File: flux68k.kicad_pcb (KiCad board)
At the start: 2 copper layers, 100 x 50 mm, 27 parts, among them J1 Conn_02x17_Odd_Even, J2 Conn_02x17_Odd_Even, J3 Conn_01x04, J4 Conn_01x04, J5 DB37_Female_MountingHoles, J6 Barrel_Jack, J7 Conn_01x01, J8 Conn_01x01, SW1 SW_SPDT, U1 74LS06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

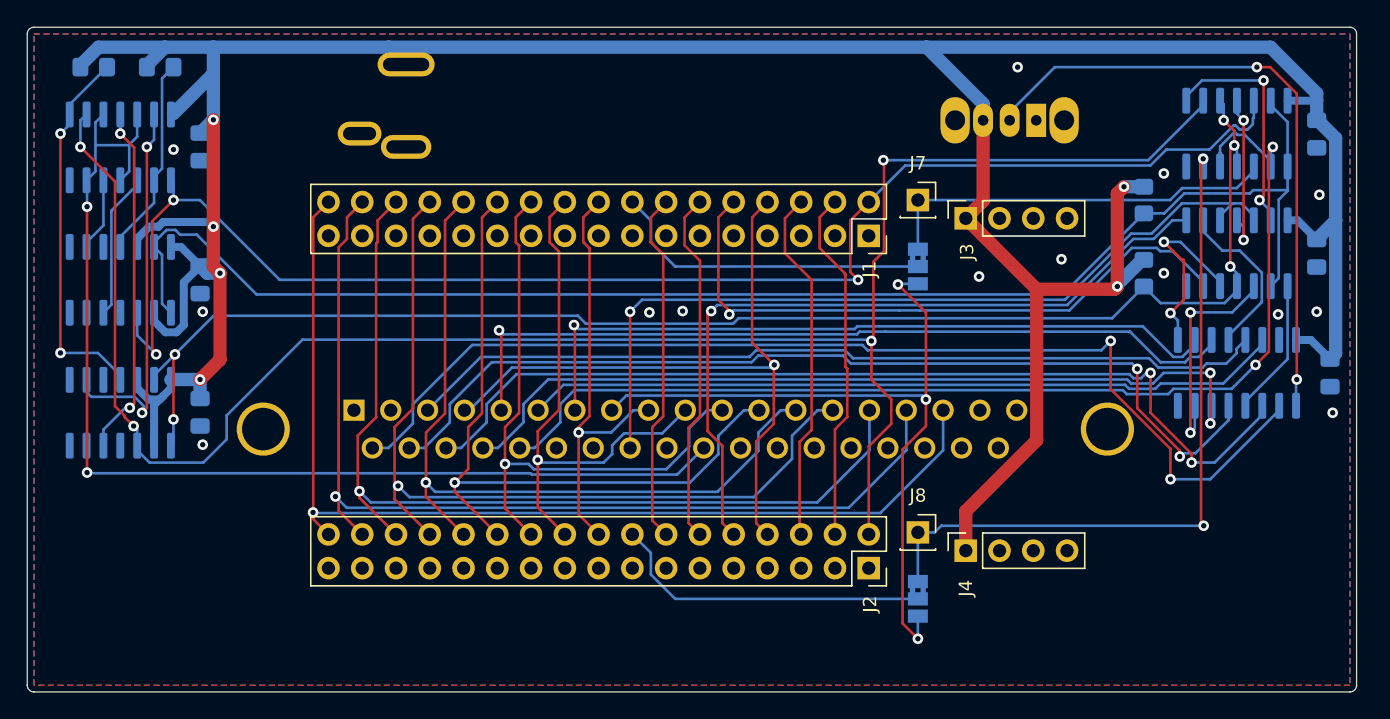
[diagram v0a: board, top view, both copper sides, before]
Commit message: add pullups and ideal diodes to flux68k
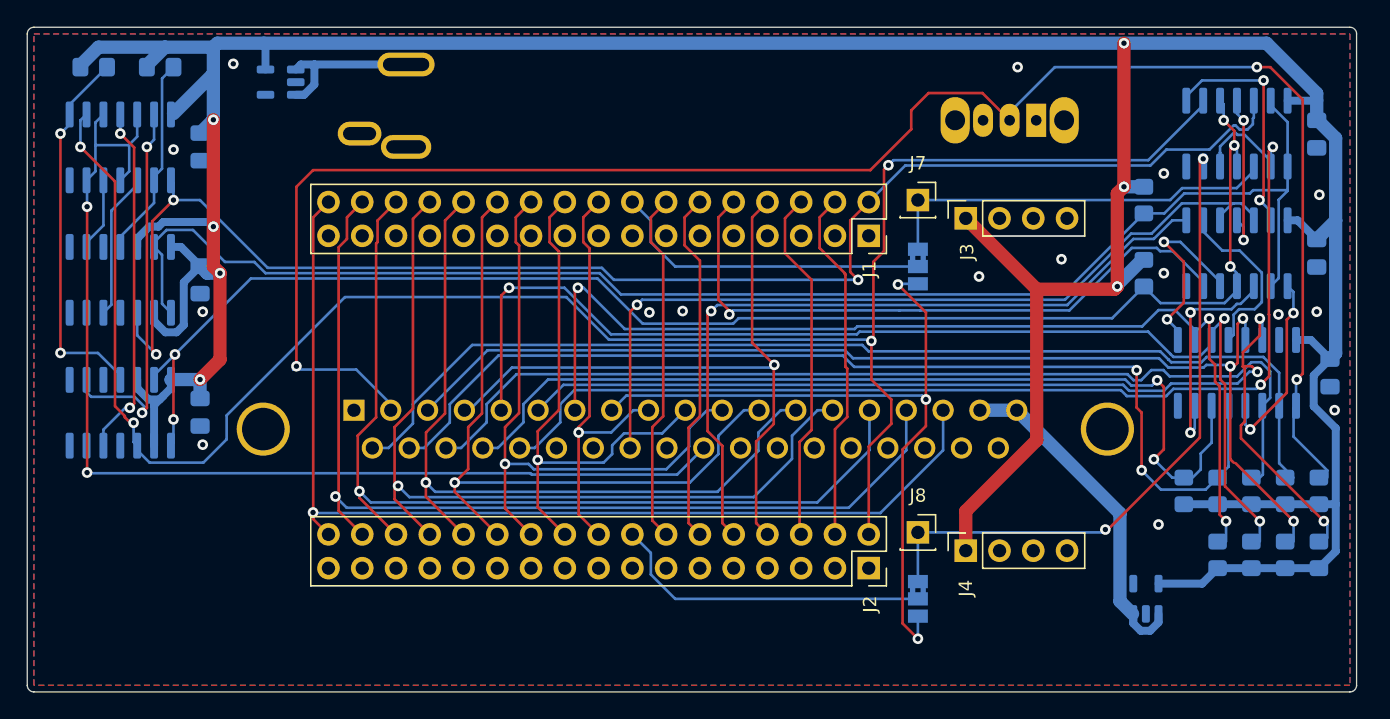
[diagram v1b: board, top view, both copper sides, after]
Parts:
- added R10: 10k, Resistor_SMD:R_0805_2012Metric_Pad1.20x1.40mm_HandSolder, B.Cu at (177.2, 59.7)
- added R11: 10k, Resistor_SMD:R_0805_2012Metric_Pad1.20x1.40mm_HandSolder, B.Cu at (169.5, 59.7)
- added R12: 10k, Resistor_SMD:R_0805_2012Metric_Pad1.20x1.40mm_HandSolder, B.Cu at (172.1, 59.7)
- added R13: 10k, Resistor_SMD:R_0805_2012Metric_Pad1.20x1.40mm_HandSolder, B.Cu at (177.2, 54.9)
- added R5: 10k, Resistor_SMD:R_0805_2012Metric_Pad1.20x1.40mm_HandSolder, B.Cu at (174.6, 54.9)
- added R6: 10k, Resistor_SMD:R_0805_2012Metric_Pad1.20x1.40mm_HandSolder, B.Cu at (172.1, 54.9)
- added R7: 10k, Resistor_SMD:R_0805_2012Metric_Pad1.20x1.40mm_HandSolder, B.Cu at (169.5, 54.9)
- added R8: 10k, Resistor_SMD:R_0805_2012Metric_Pad1.20x1.40mm_HandSolder, B.Cu at (167.0, 54.9)
- added R9: 10k, Resistor_SMD:R_0805_2012Metric_Pad1.20x1.40mm_HandSolder, B.Cu at (174.6, 59.7)
- added U7: MAX40200AUK, Package_TO_SOT_SMD:SOT-23-5, B.Cu at (99.1, 24.1)
- added U8: MAX40200AUK, Package_TO_SOT_SMD:SOT-23-5, B.Cu at (164.2, 63.0)
- U2: value 74LS32 -> 74HCT32
- U3, U4: value 74LS74 -> 74HCT74
- U6: value 74LS157 -> 74HCT157
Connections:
- J5 pad 18: unconnected-(J5-Pad18) -> /VIN_DB37
- J5 pad 19: unconnected-(J5-Pad19) -> /VIN_DB37
- J5 pad 2: unconnected-(J5-Pad2) -> /~{SWAP}
- J6 pad 1: +5V -> /VIN_BARREL
- SW1 pad 2: Net-(SW1-Pad2) -> /~{SWAP}
- SW1 pad 3: +5V -> unconnected-(SW1-C-Pad3)
- U6 pad 1: Net-(SW1-Pad2) -> /~{SWAP}
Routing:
- net /~{SWAP}: track 0.00 -> 136.0 mm, vias 0 -> 3
- net Net-(SW1-Pad2): track 47.9 -> 0.00 mm, vias 2 -> 0
- net +5V: track 256.4 -> 293.9 mm, vias 6 -> 7
- net /VIN_DB37: track 0.00 -> 25.4 mm
- net /~{X68K_DS0}: track 61.7 -> 85.5 mm, vias 1 -> 3
- net /~{X68K_DS2}: track 55.0 -> 78.3 mm, vias 1 -> 3
- net /~{X68K_DS1}: track 57.1 -> 78.5 mm, vias 0 -> 3
- net /~{X68K_DS3}: track 65.0 -> 83.8 mm, vias 0 -> 3
- net /VIN_BARREL: track 0.00 -> 11.7 mm
- net /~{OPTION1}: track 72.7 -> 79.0 mm
- net /~{OPTION3}: track 63.3 -> 69.3 mm
- net /~{BOTTOM_EJECT}: track 53.7 -> 49.5 mm
- net Net-(U6-Za): track 10.3 -> 14.2 mm, vias 0 -> 2
- net /~{OPTION2}: track 71.9 -> 74.9 mm, vias 2 -> 0
- net /~{BOTTOM_DCD}: track 143.8 -> 146.2 mm
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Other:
- board text added: "TD-FluX68K v1.1"
- board text removed: "TD-FluX68K v1.0"

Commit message: shrink board by 1mm
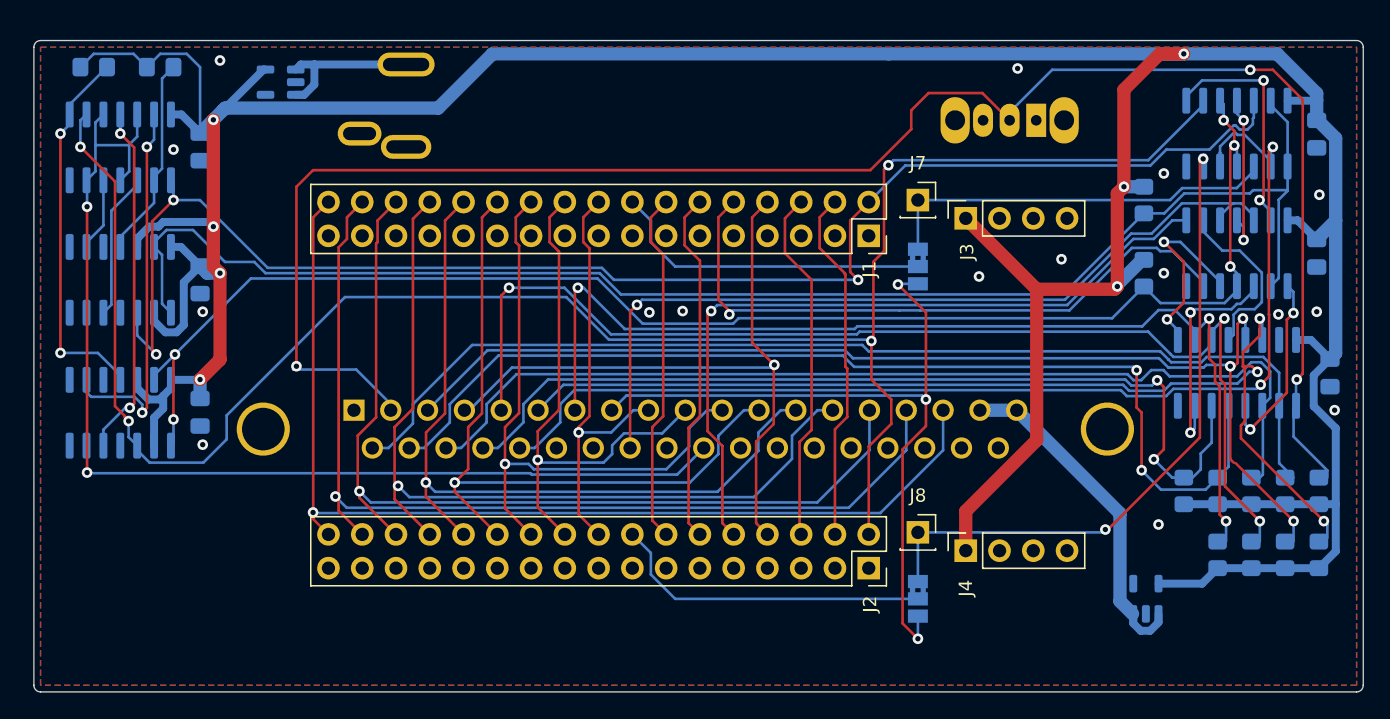
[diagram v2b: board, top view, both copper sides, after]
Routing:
- net +5V: track 293.9 -> 296.0 mm
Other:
- board size 100 x 50 mm -> 100 x 49 mm
